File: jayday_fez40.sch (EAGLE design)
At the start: 52 parts, among them IC1 GHI_STM32F40X, IC2 LM1117MP-3.3, IC9 MIC4680-ADJ, Q2 32.768Khz, U3 MICROSD_MICROSD, X4 DX2R005HN2E700

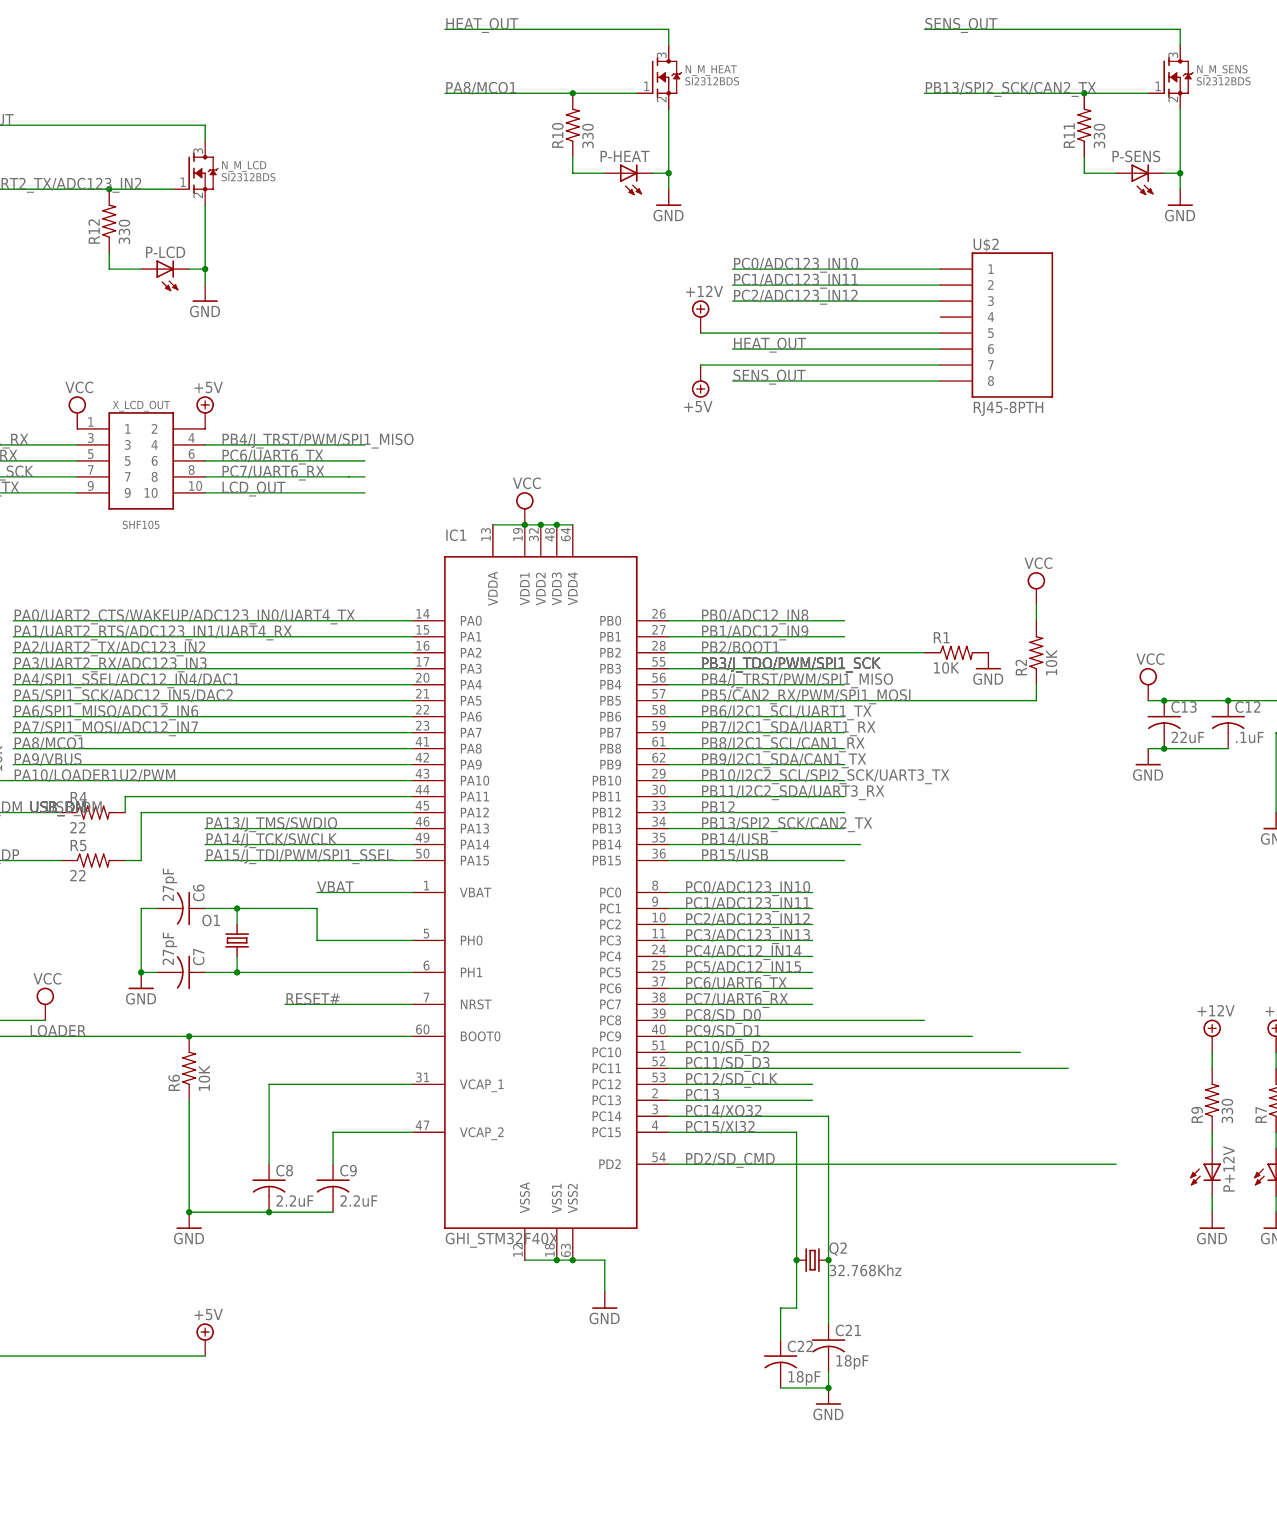
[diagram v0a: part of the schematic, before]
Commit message: layed out board.. 2 traces left
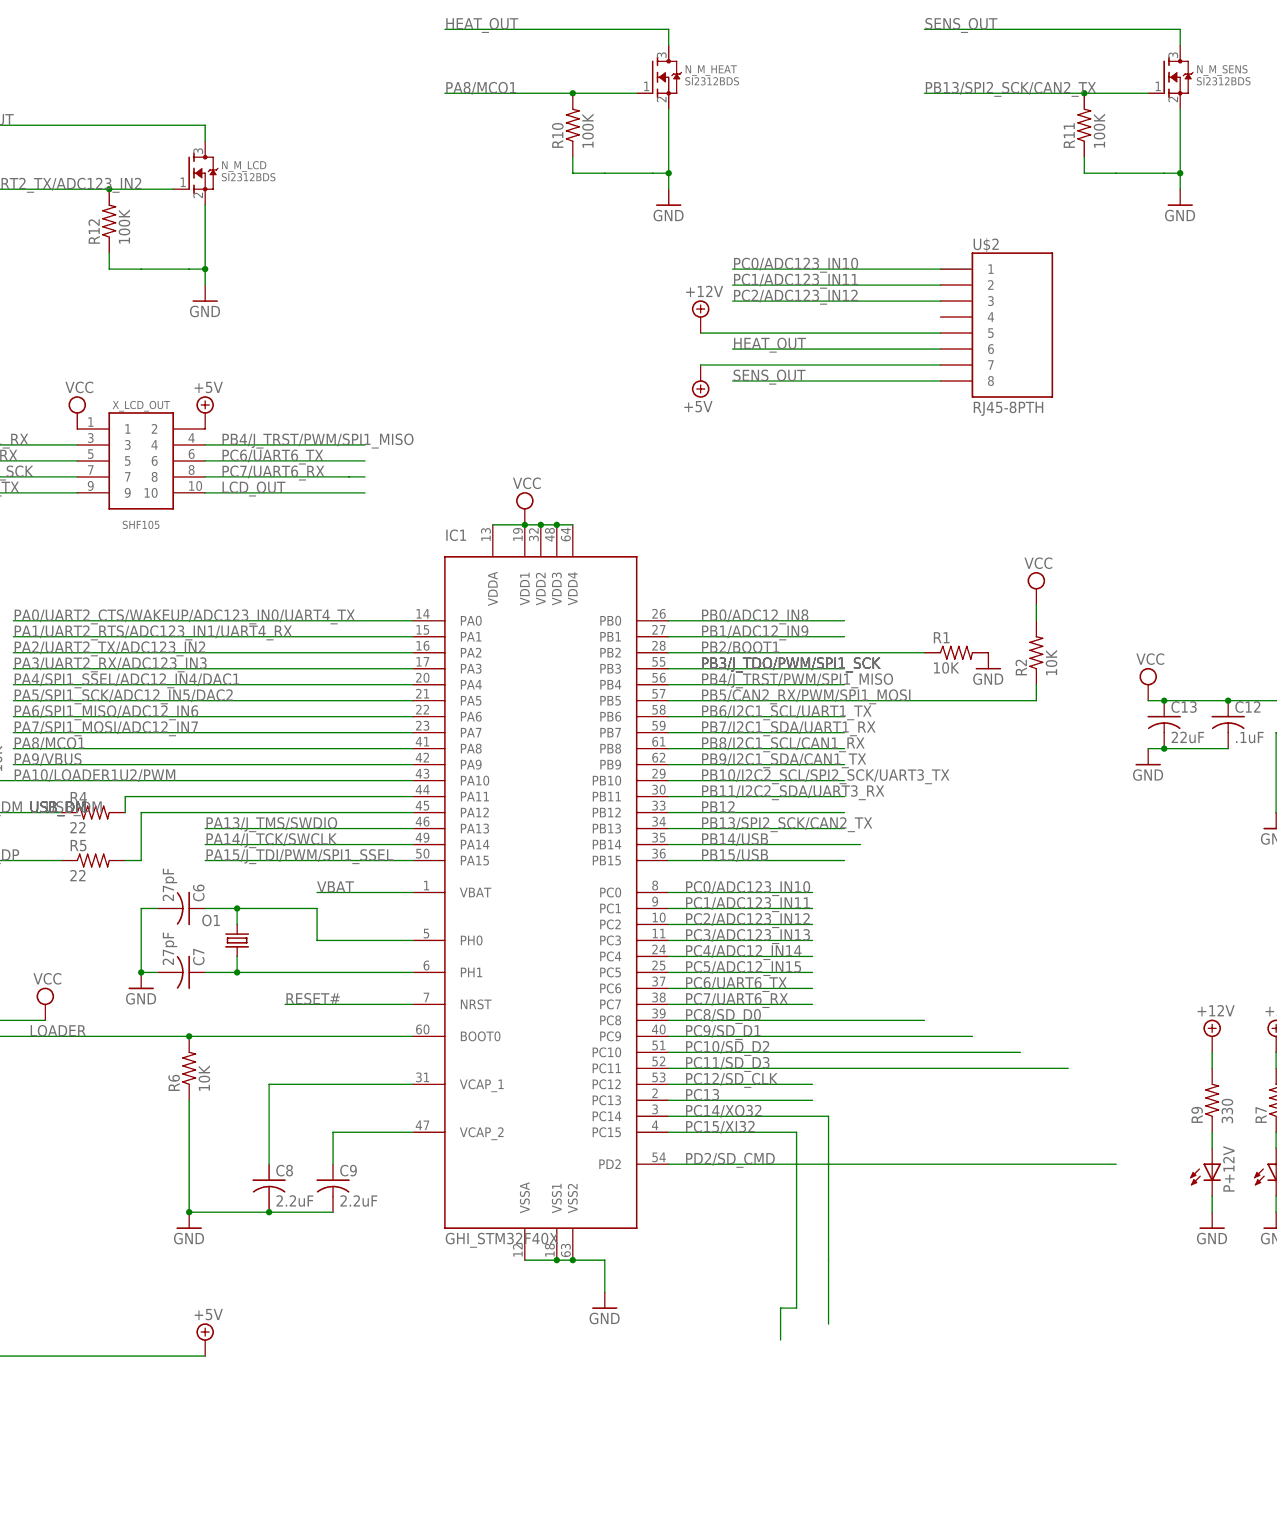
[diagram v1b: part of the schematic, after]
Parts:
- removed C21, C22: 18pF, rcl:C-USC0603K
- removed P-HEAT, P-LCD, P-SENS: (no value), led:LEDCHIPLED_0805
- removed Q2: 32.768Khz, crystal:CRYSTALTC38H
- R10, R11, R12: value 330 -> 100K
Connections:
- removed net N$14: P-HEAT.A, R10.1
- removed net N$15: P-SENS.A, R11.1
- removed net N$16: P-LCD.A, R12.1
- net GND: now also R10.1, R11.1, R12.1; no longer C21.2, C22.2, P-HEAT.C, P-LCD.C, P-SENS.C
- net PC14/XO32: no longer C21.1, Q2.2
- net PC15/XI32: no longer C22.1, Q2.1
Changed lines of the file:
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@@
 <part name="R4" library="rcl" deviceset="R-US_" device="R0603" value="22"/>
 <part name="R5" library="rcl" deviceset="R-US_" device="R0603" value="22"/>
-<part name="C21" library="rcl" deviceset="C-US" device="C0603K" value="18pF"/>
-<part name="C22" library="rcl" deviceset="C-US" device="C0603K" value="18pF"/>
-<part name="GND22" library="supply1" deviceset="GND" device=""/>
-<part name="Q2" library="crystal" deviceset="CRYSTAL" device="TC38H" value="32.768Khz"/>
 <part name="R2" library="rcl" deviceset="R-US_" device="R0603" value="10K"/>
 <part name="V6" library="supply2" deviceset="VCC" device=""/>
@@
 <part name="SUPPLY12" library="supply2" deviceset="+12V" device=""/>
 <part name="GND12" library="supply1" deviceset="GND" device=""/>
-<part name="P-HEAT" library="led" deviceset="LED" device="CHIPLED_0805"/>
-<part name="R10" library="rcl" deviceset="R-US_" device="R0603" value="330"/>
+<part name="R10" library="rcl" deviceset="R-US_" device="R0603" value="100K"/>
 <part name="GND13" library="supply1" deviceset="GND" device=""/>
-<part name="P-SENS" library="led" deviceset="LED" device="CHIPLED_0805"/>
-<part name="R11" library="rcl" deviceset="R-US_" device="R0603" value="330"/>
+<part name="R11" library="rcl" deviceset="R-US_" device="R0603" value="100K"/>
 <part name="SUPPLY13" library="supply2" deviceset="+5V" device=""/>
 <part name="SUPPLY15" library="supply2" deviceset="VCC" device=""/>
 <part name="N_M_LCD" library="ozlollc" deviceset="SI2312BDS" device=""/>
 <part name="GND15" library="supply1" deviceset="GND" device=""/>
-<part name="P-LCD" library="led" deviceset="LED" device="CHIPLED_0805"/>
-<part name="R12" library="rcl" deviceset="R-US_" device="R0603" value="330"/>
+<part name="R12" library="rcl" deviceset="R-US_" device="R0603" value="100K"/>
 <part name="U3" library="FEZ_Panda" deviceset="MICROSD_MICROSD" device=""/>
 <part name="GND16" library="supply1" deviceset="GND" device=""/>
@@
 <instance part="R4" gate="G$1" x="15.24" y="48.26"/>
 <instance part="R5" gate="G$1" x="15.24" y="40.64"/>
-<instance part="C21" gate="G$1" x="132.08" y="-35.56"/>
-<instance part="C22" gate="G$1" x="124.46" y="-38.1"/>
-<instance part="GND22" gate="1" x="132.08" y="-45.72"/>
-<instance part="Q2" gate="G$1" x="129.54" y="-22.86"/>
 <instance part="R2" gate="G$1" x="165.1" y="73.66" rot="R90"/>
 <instance part="V6" gate="G$1" x="165.1" y="83.82"/>
@@
 <instance part="SUPPLY12" gate="+12V" x="111.76" y="127"/>
 <instance part="GND12" gate="1" x="106.68" y="144.78"/>
-<instance part="P-HEAT" gate="G$1" x="99.06" y="149.86" rot="R90"/>
 <instance part="R10" gate="G$1" x="91.44" y="157.48" rot="R90"/>
 <instance part="GND13" gate="1" x="187.96" y="144.78"/>
-<instance part="P-SENS" gate="G$1" x="180.34" y="149.86" rot="R90"/>
 <instance part="R11" gate="G$1" x="172.72" y="157.48" rot="R90"/>
 <instance part="SUPPLY13" gate="+5V" x="33.02" y="111.76"/>
@@
 <instance part="N_M_LCD" gate="G$1" x="33.02" y="149.86"/>
 <instance part="GND15" gate="1" x="33.02" y="129.54"/>
-<instance part="P-LCD" gate="G$1" x="25.4" y="134.62" rot="R90"/>
 <instance part="R12" gate="G$1" x="17.78" y="142.24" rot="R90"/>
 <instance part="U3" gate="G$1" x="248.92" y="58.42"/>
@@
 <pinref part="C6" gate="G$1" pin="2"/>
 <pinref part="GND6" gate="1" pin="GND"/>
-</segment>
-<segment>
-<wire x1="124.46" y1="-43.18" x2="132.08" y2="-43.18" width="0.1524" layer="91"/>
-<wire x1="132.08" y1="-43.18" x2="132.08" y2="-40.64" width="0.1524" layer="91"/>
-<junction x="132.08" y="-43.18"/>
-<pinref part="C22" gate="G$1" pin="2"/>
-<pinref part="C21" gate="G$1" pin="2"/>
-<pinref part="GND22" gate="1" pin="GND"/>
 </segment>
 <segment>
@@
 <pinref part="N_M_HEAT" gate="G$1" pin="S"/>
 <wire x1="106.68" y1="160.02" x2="106.68" y2="149.86" width="0.1524" layer="91"/>
-<pinref part="P-HEAT" gate="G$1" pin="C"/>
 <wire x1="106.68" y1="149.86" x2="106.68" y2="147.32" width="0.1524" layer="91"/>
 <wire x1="104.14" y1="149.86" x2="106.68" y2="149.86" width="0.1524" layer="91"/>
 <junction x="106.68" y="149.86"/>
+<pinref part="R10" gate="G$1" pin="1"/>
+<wire x1="91.44" y1="152.4" x2="91.44" y2="149.86" width="0.1524" layer="91"/>
+<wire x1="91.44" y1="149.86" x2="96.52" y2="149.86" width="0.1524" layer="91"/>
+<wire x1="96.52" y1="149.86" x2="104.14" y2="149.86" width="0.1524" layer="91"/>
 </segment>
 <segment>
 <pinref part="GND13" gate="1" pin="GND"/>
 <wire x1="187.96" y1="160.02" x2="187.96" y2="149.86" width="0.1524" layer="91"/>
-<pinref part="P-SENS" gate="G$1" pin="C"/>
 <wire x1="187.96" y1="149.86" x2="187.96" y2="147.32" width="0.1524" layer="91"/>
 <wire x1="185.42" y1="149.86" x2="187.96" y2="149.86" width="0.1524" layer="91"/>
 <junction x="187.96" y="149.86"/>
 <pinref part="N_M_SENS" gate="G$1" pin="S"/>
+<pinref part="R11" gate="G$1" pin="1"/>
+<wire x1="172.72" y1="152.4" x2="172.72" y2="149.86" width="0.1524" layer="91"/>
+<wire x1="172.72" y1="149.86" x2="177.8" y2="149.86" width="0.1524" layer="91"/>
+<wire x1="177.8" y1="149.86" x2="185.42" y2="149.86" width="0.1524" layer="91"/>
 </segment>
 <segment>
 <pinref part="GND15" gate="1" pin="GND"/>
 <wire x1="33.02" y1="144.78" x2="33.02" y2="134.62" width="0.1524" layer="91"/>
-<pinref part="P-LCD" gate="G$1" pin="C"/>
 <wire x1="33.02" y1="134.62" x2="33.02" y2="132.08" width="0.1524" layer="91"/>
 <wire x1="30.48" y1="134.62" x2="33.02" y2="134.62" width="0.1524" layer="91"/>
 <junction x="33.02" y="134.62"/>
 <pinref part="N_M_LCD" gate="G$1" pin="S"/>
+<pinref part="R12" gate="G$1" pin="1"/>
+<wire x1="17.78" y1="137.16" x2="17.78" y2="134.62" width="0.1524" layer="91"/>
+<wire x1="17.78" y1="134.62" x2="22.86" y2="134.62" width="0.1524" layer="91"/>
+<wire x1="22.86" y1="134.62" x2="30.48" y2="134.62" width="0.1524" layer="91"/>
 </segment>
 <segment>
@@
 <wire x1="127" y1="-30.48" x2="127" y2="-22.86" width="0.1524" layer="91"/>
 <wire x1="127" y1="-22.86" x2="127" y2="-2.54" width="0.1524" layer="91"/>
-<junction x="127" y="-22.86"/>
 <label x="109.22" y="-2.54" size="1.778" layer="95"/>
-<pinref part="C22" gate="G$1" pin="1"/>
-<pinref part="Q2" gate="G$1" pin="1"/>
 <pinref part="IC1" gate="G$1" pin="PC15"/>
 </segment>
@@
 <wire x1="132.08" y1="-33.02" x2="132.08" y2="-22.86" width="0.1524" layer="91"/>
 <wire x1="132.08" y1="-22.86" x2="132.08" y2="0" width="0.1524" layer="91"/>
-<junction x="132.08" y="-22.86"/>
 <label x="109.22" y="0" size="1.778" layer="95"/>
-<pinref part="C21" gate="G$1" pin="1"/>
-<pinref part="Q2" gate="G$1" pin="2"/>
 <pinref part="IC1" gate="G$1" pin="PC14"/>
 </segment>
@@
 </segment>
 </net>
-<net name="N$14" class="0">
-<segment>
-<pinref part="R10" gate="G$1" pin="1"/>
-<pinref part="P-HEAT" gate="G$1" pin="A"/>
-<wire x1="91.44" y1="152.4" x2="91.44" y2="149.86" width="0.1524" layer="91"/>
-<wire x1="91.44" y1="149.86" x2="96.52" y2="149.86" width="0.1524" layer="91"/>
-</segment>
-</net>
 <net name="HEAT_OUT" class="0">
 <segment>
@@
 </segment>
 </net>
-<net name="N$15" class="0">
-<segment>
-<pinref part="R11" gate="G$1" pin="1"/>
-<pinref part="P-SENS" gate="G$1" pin="A"/>
-<wire x1="172.72" y1="152.4" x2="172.72" y2="149.86" width="0.1524" layer="91"/>
-<wire x1="172.72" y1="149.86" x2="177.8" y2="149.86" width="0.1524" layer="91"/>
-</segment>
-</net>
 <net name="SENS_OUT" class="0">
 <segment>
@@
 </segment>
 </net>
-<net name="N$16" class="0">
-<segment>
-<pinref part="R12" gate="G$1" pin="1"/>
-<pinref part="P-LCD" gate="G$1" pin="A"/>
-<wire x1="17.78" y1="137.16" x2="17.78" y2="134.62" width="0.1524" layer="91"/>
-<wire x1="17.78" y1="134.62" x2="22.86" y2="134.62" width="0.1524" layer="91"/>
-</segment>
-</net>
